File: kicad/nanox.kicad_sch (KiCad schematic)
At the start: 138 parts, among them P1 likely an ESD protection diod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, P2 likely an ESD protection diod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, P3 likely an ESD protection diod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, P4 likely an ESD protection diod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, P5 likely an ESD protection diod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, SW1 push button, left, SW2 push button, right, X1 ?, X10 unknown, marked 1C4F, likely 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, X2 unknown, marked 2GC, X3 unknown, marked 6, X4 ?, X5 ?, X6 ?, X7 ?, X8 ?, X9 unknown, marked P8W 26, Y1 crystal, likely the 32 MHz HSE

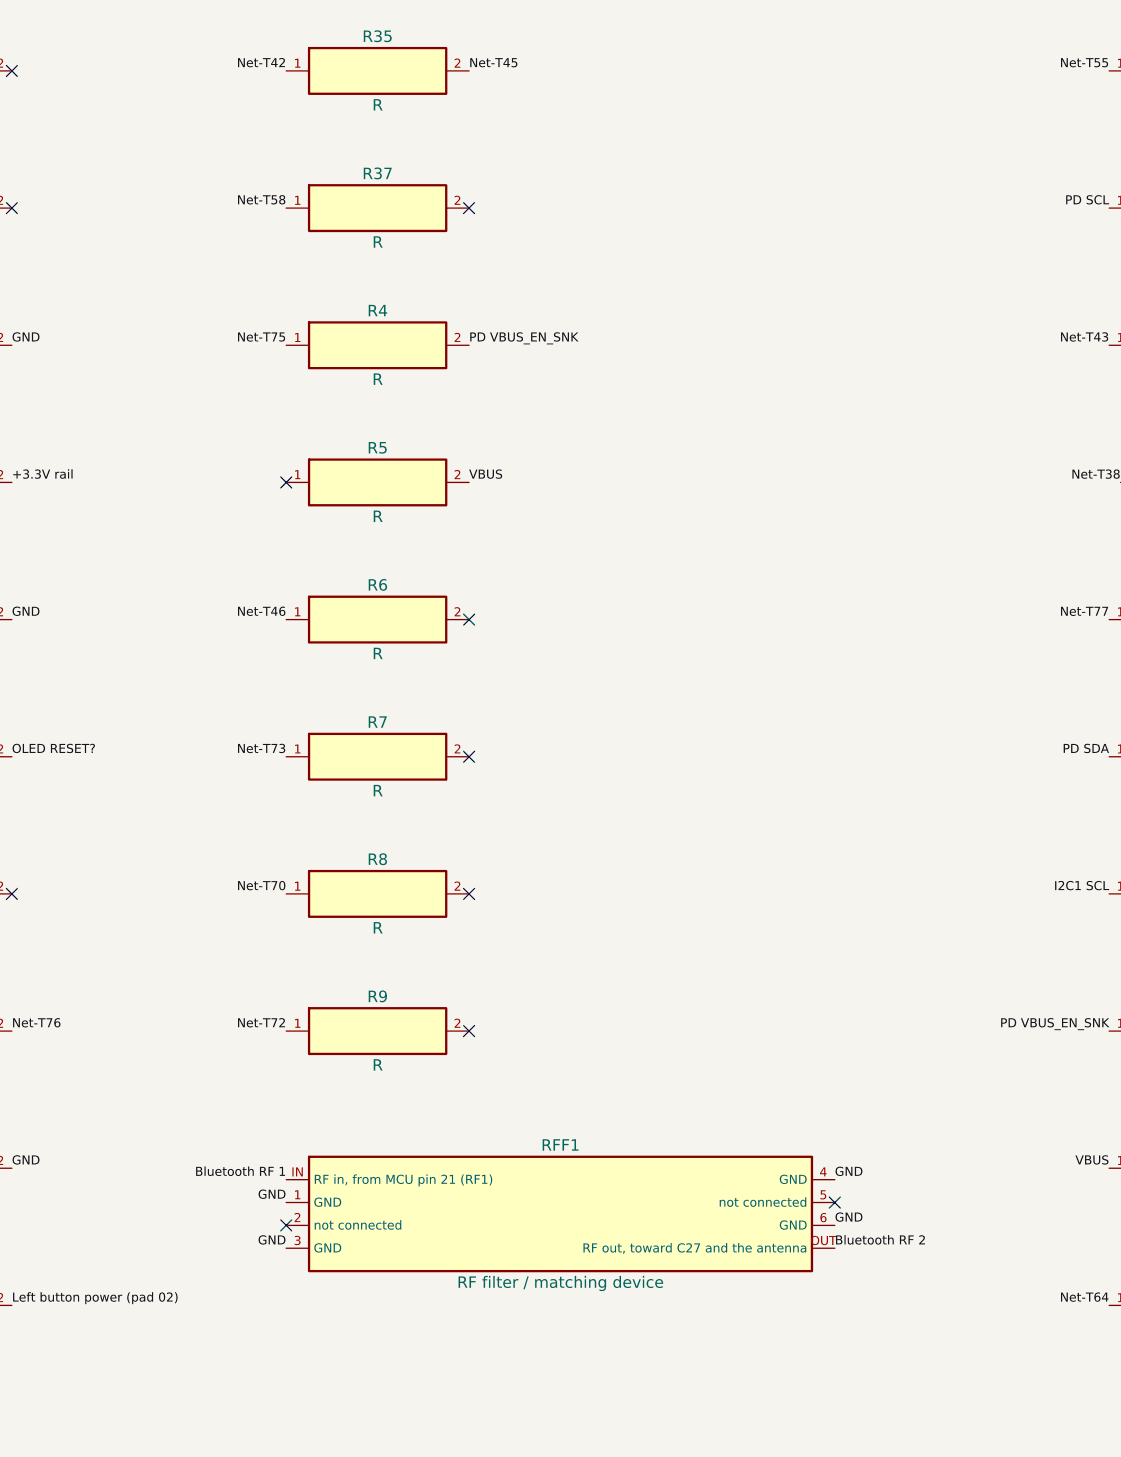
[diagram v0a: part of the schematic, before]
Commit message: Remove R37, a duplicate of R19
R37 was added by hand on the resistor below R18, which the automatic
pass had already found as R19. R19 keeps R37's better-fitting box.

Co-Authored-By: Claude Opus 5.5 <noreply@anthropic.com>
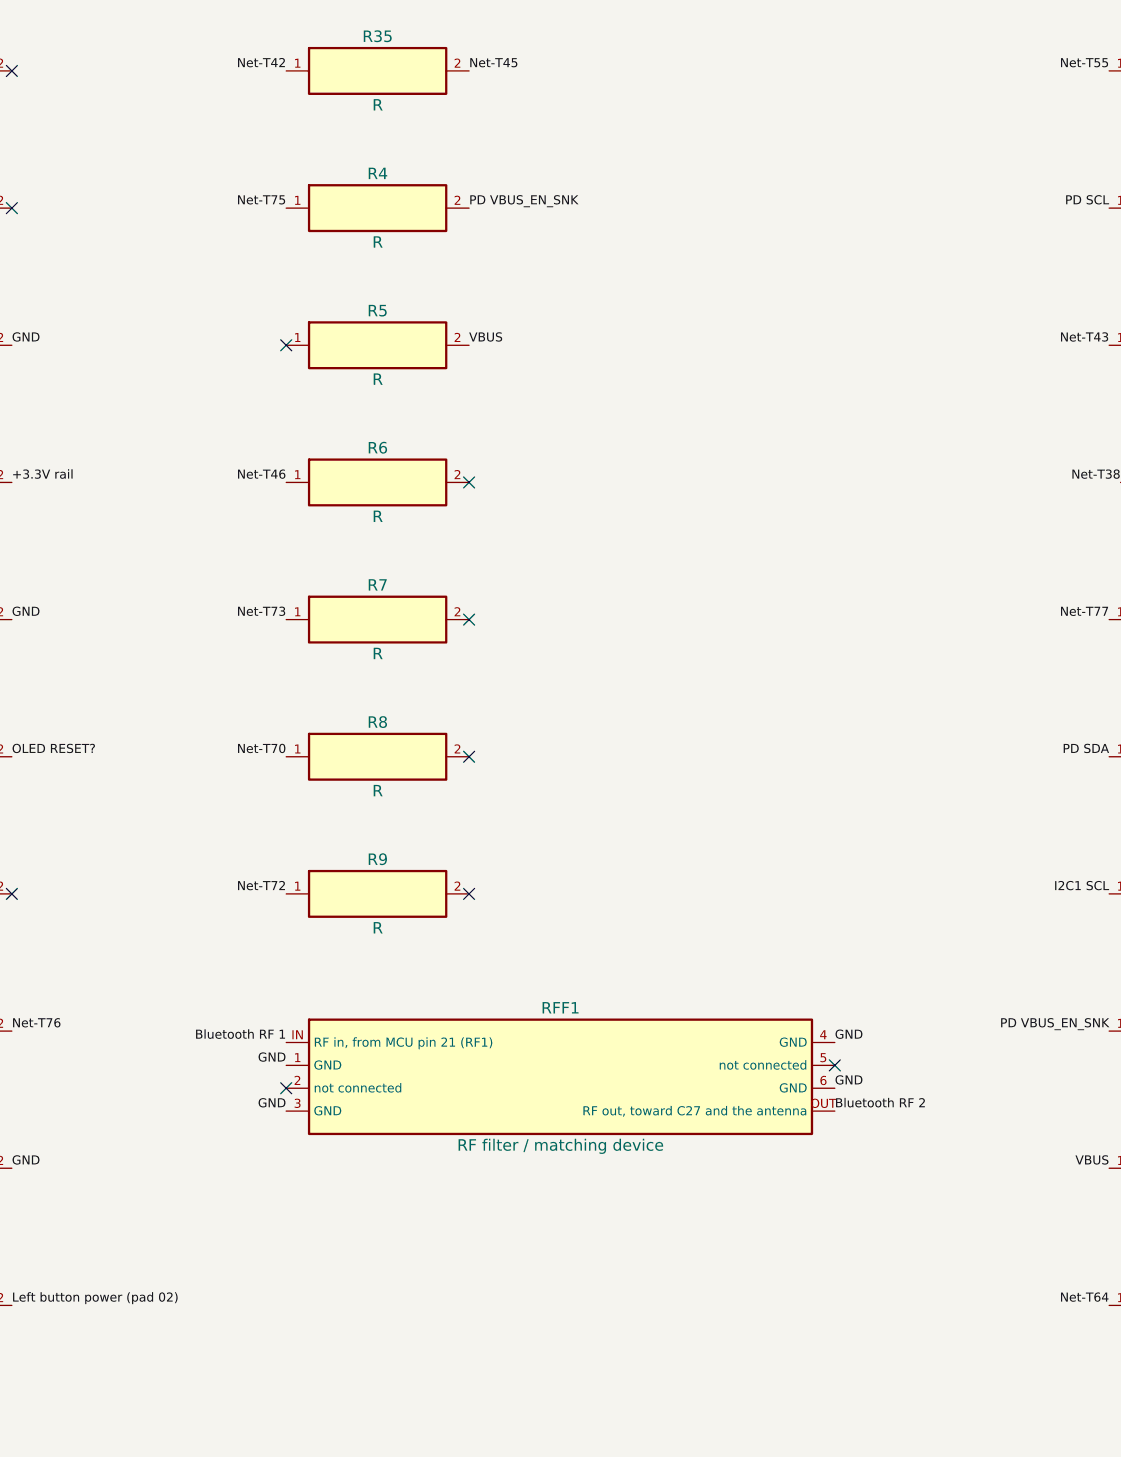
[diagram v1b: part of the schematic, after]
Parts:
- removed R37: R, symbol nanox:R37
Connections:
- no-connect marks 73 -> 72
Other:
- moved on the sheet: R4, R5, R6, R7, R8, R9, RFF1
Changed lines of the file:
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@@
  (label "Net-T42" (at 236.22 149.86 180) (effects (font (size 1.0 1.0)) (justify right bottom)))
  (label "Net-T45" (at 256.54 149.86 0) (effects (font (size 1.0 1.0)) (justify left bottom)))
- (symbol (lib_id "nanox:R37") (at 246.38 165.10 0) (unit 1) (in_bom yes) (on_board yes) (dnp no)
-  (property "Reference" "R37" (at 246.38 161.29 0) (effects (font (size 1.27 1.27))))
+ (symbol (lib_id "nanox:R4") (at 246.38 165.10 0) (unit 1) (in_bom yes) (on_board yes) (dnp no)
+  (property "Reference" "R4" (at 246.38 161.29 0) (effects (font (size 1.27 1.27))))
   (property "Value" "R" (at 246.38 168.91 0) (effects (font (size 1.27 1.27))))
   (property "Footprint" "" (at 246.38 165.10 0) (effects (font (size 1.27 1.27)) hide))
@@
   (pin "1")
   (pin "2")
-  (instances (project "nanox" (path "/9fc871f3-1e36-5a01-9359-e2a20c86f96f" (reference "R37") (unit 1))))
+  (instances (project "nanox" (path "/9fc871f3-1e36-5a01-9359-e2a20c86f96f" (reference "R4") (unit 1))))
  )
- (label "Net-T58" (at 236.22 165.10 180) (effects (font (size 1.0 1.0)) (justify right bottom)))
- (no_connect (at 256.54 165.10))
- (symbol (lib_id "nanox:R4") (at 246.38 180.34 0) (unit 1) (in_bom yes) (on_board yes) (dnp no)
-  (property "Reference" "R4" (at 246.38 176.53 0) (effects (font (size 1.27 1.27))))
+ (label "Net-T75" (at 236.22 165.10 180) (effects (font (size 1.0 1.0)) (justify right bottom)))
+ (label "PD VBUS_EN_SNK" (at 256.54 165.10 0) (effects (font (size 1.0 1.0)) (justify left bottom)))
+ (symbol (lib_id "nanox:R5") (at 246.38 180.34 0) (unit 1) (in_bom yes) (on_board yes) (dnp no)
+  (property "Reference" "R5" (at 246.38 176.53 0) (effects (font (size 1.27 1.27))))
   (property "Value" "R" (at 246.38 184.15 0) (effects (font (size 1.27 1.27))))
   (property "Footprint" "" (at 246.38 180.34 0) (effects (font (size 1.27 1.27)) hide))
@@
   (pin "1")
   (pin "2")
-  (instances (project "nanox" (path "/9fc871f3-1e36-5a01-9359-e2a20c86f96f" (reference "R4") (unit 1))))
+  (instances (project "nanox" (path "/9fc871f3-1e36-5a01-9359-e2a20c86f96f" (reference "R5") (unit 1))))
  )
- (label "Net-T75" (at 236.22 180.34 180) (effects (font (size 1.0 1.0)) (justify right bottom)))
- (label "PD VBUS_EN_SNK" (at 256.54 180.34 0) (effects (font (size 1.0 1.0)) (justify left bottom)))
- (symbol (lib_id "nanox:R5") (at 246.38 195.58 0) (unit 1) (in_bom yes) (on_board yes) (dnp no)
-  (property "Reference" "R5" (at 246.38 191.77 0) (effects (font (size 1.27 1.27))))
+ (no_connect (at 236.22 180.34))
+ (label "VBUS" (at 256.54 180.34 0) (effects (font (size 1.0 1.0)) (justify left bottom)))
+ (symbol (lib_id "nanox:R6") (at 246.38 195.58 0) (unit 1) (in_bom yes) (on_board yes) (dnp no)
+  (property "Reference" "R6" (at 246.38 191.77 0) (effects (font (size 1.27 1.27))))
   (property "Value" "R" (at 246.38 199.39 0) (effects (font (size 1.27 1.27))))
   (property "Footprint" "" (at 246.38 195.58 0) (effects (font (size 1.27 1.27)) hide))
@@
   (pin "1")
   (pin "2")
-  (instances (project "nanox" (path "/9fc871f3-1e36-5a01-9359-e2a20c86f96f" (reference "R5") (unit 1))))
+  (instances (project "nanox" (path "/9fc871f3-1e36-5a01-9359-e2a20c86f96f" (reference "R6") (unit 1))))
  )
- (no_connect (at 236.22 195.58))
- (label "VBUS" (at 256.54 195.58 0) (effects (font (size 1.0 1.0)) (justify left bottom)))
- (symbol (lib_id "nanox:R6") (at 246.38 210.82 0) (unit 1) (in_bom yes) (on_board yes) (dnp no)
-  (property "Reference" "R6" (at 246.38 207.01 0) (effects (font (size 1.27 1.27))))
+ (label "Net-T46" (at 236.22 195.58 180) (effects (font (size 1.0 1.0)) (justify right bottom)))
+ (no_connect (at 256.54 195.58))
+ (symbol (lib_id "nanox:R7") (at 246.38 210.82 0) (unit 1) (in_bom yes) (on_board yes) (dnp no)
+  (property "Reference" "R7" (at 246.38 207.01 0) (effects (font (size 1.27 1.27))))
   (property "Value" "R" (at 246.38 214.63 0) (effects (font (size 1.27 1.27))))
   (property "Footprint" "" (at 246.38 210.82 0) (effects (font (size 1.27 1.27)) hide))
@@
   (pin "1")
   (pin "2")
-  (instances (project "nanox" (path "/9fc871f3-1e36-5a01-9359-e2a20c86f96f" (reference "R6") (unit 1))))
+  (instances (project "nanox" (path "/9fc871f3-1e36-5a01-9359-e2a20c86f96f" (reference "R7") (unit 1))))
  )
- (label "Net-T46" (at 236.22 210.82 180) (effects (font (size 1.0 1.0)) (justify right bottom)))
+ (label "Net-T73" (at 236.22 210.82 180) (effects (font (size 1.0 1.0)) (justify right bottom)))
  (no_connect (at 256.54 210.82))
- (symbol (lib_id "nanox:R7") (at 246.38 226.06 0) (unit 1) (in_bom yes) (on_board yes) (dnp no)
-  (property "Reference" "R7" (at 246.38 222.25 0) (effects (font (size 1.27 1.27))))
+ (symbol (lib_id "nanox:R8") (at 246.38 226.06 0) (unit 1) (in_bom yes) (on_board yes) (dnp no)
+  (property "Reference" "R8" (at 246.38 222.25 0) (effects (font (size 1.27 1.27))))
   (property "Value" "R" (at 246.38 229.87 0) (effects (font (size 1.27 1.27))))
   (property "Footprint" "" (at 246.38 226.06 0) (effects (font (size 1.27 1.27)) hide))
@@
   (pin "1")
   (pin "2")
-  (instances (project "nanox" (path "/9fc871f3-1e36-5a01-9359-e2a20c86f96f" (reference "R7") (unit 1))))
+  (instances (project "nanox" (path "/9fc871f3-1e36-5a01-9359-e2a20c86f96f" (reference "R8") (unit 1))))
  )
- (label "Net-T73" (at 236.22 226.06 180) (effects (font (size 1.0 1.0)) (justify right bottom)))
+ (label "Net-T70" (at 236.22 226.06 180) (effects (font (size 1.0 1.0)) (justify right bottom)))
  (no_connect (at 256.54 226.06))
- (symbol (lib_id "nanox:R8") (at 246.38 241.30 0) (unit 1) (in_bom yes) (on_board yes) (dnp no)
-  (property "Reference" "R8" (at 246.38 237.49 0) (effects (font (size 1.27 1.27))))
+ (symbol (lib_id "nanox:R9") (at 246.38 241.30 0) (unit 1) (in_bom yes) (on_board yes) (dnp no)
+  (property "Reference" "R9" (at 246.38 237.49 0) (effects (font (size 1.27 1.27))))
   (property "Value" "R" (at 246.38 245.11 0) (effects (font (size 1.27 1.27))))
   (property "Footprint" "" (at 246.38 241.30 0) (effects (font (size 1.27 1.27)) hide))
@@
   (pin "1")
   (pin "2")
-  (instances (project "nanox" (path "/9fc871f3-1e36-5a01-9359-e2a20c86f96f" (reference "R8") (unit 1))))
- )
- (label "Net-T70" (at 236.22 241.30 180) (effects (font (size 1.0 1.0)) (justify right bottom)))
- (no_connect (at 256.54 241.30))
- (symbol (lib_id "nanox:R9") (at 246.38 256.54 0) (unit 1) (in_bom yes) (on_board yes) (dnp no)
-  (property "Reference" "R9" (at 246.38 252.73 0) (effects (font (size 1.27 1.27))))
-  (property "Value" "R" (at 246.38 260.35 0) (effects (font (size 1.27 1.27))))
-  (property "Footprint" "" (at 246.38 256.54 0) (effects (font (size 1.27 1.27)) hide))
-  (property "Description" "two-terminal SMD" (at 246.38 256.54 0) (effects (font (size 1.27 1.27)) hide))
-  (pin "1")
-  (pin "2")
   (instances (project "nanox" (path "/9fc871f3-1e36-5a01-9359-e2a20c86f96f" (reference "R9") (unit 1))))
  )
- (label "Net-T72" (at 236.22 256.54 180) (effects (font (size 1.0 1.0)) (justify right bottom)))
- (no_connect (at 256.54 256.54))
- (symbol (lib_id "nanox:RFF1") (at 266.70 276.86 0) (unit 1) (in_bom yes) (on_board yes) (dnp no)
-  (property "Reference" "RFF1" (at 266.70 269.24 0) (effects (font (size 1.27 1.27))))
-  (property "Value" "RF filter / matching device" (at 266.70 284.48 0) (effects (font (size 1.27 1.27))))
-  (property "Footprint" "" (at 266.70 276.86 0) (effects (font (size 1.27 1.27)) hide))
-  (property "Description" "blue ceramic, 8 terminals" (at 266.70 276.86 0) (effects (font (size 1.27 1.27)) hide))
+ (label "Net-T72" (at 236.22 241.30 180) (effects (font (size 1.0 1.0)) (justify right bottom)))
+ (no_connect (at 256.54 241.30))
+ (symbol (lib_id "nanox:RFF1") (at 266.70 261.62 0) (unit 1) (in_bom yes) (on_board yes) (dnp no)
+  (property "Reference" "RFF1" (at 266.70 254.00 0) (effects (font (size 1.27 1.27))))
+  (property "Value" "RF filter / matching device" (at 266.70 269.24 0) (effects (font (size 1.27 1.27))))
+  (property "Footprint" "" (at 266.70 261.62 0) (effects (font (size 1.27 1.27)) hide))
+  (property "Description" "blue ceramic, 8 terminals" (at 266.70 261.62 0) (effects (font (size 1.27 1.27)) hide))
   (pin "IN")
   (pin "1")
@@
   (instances (project "nanox" (path "/9fc871f3-1e36-5a01-9359-e2a20c86f96f" (reference "RFF1") (unit 1))))
  )
- (label "Bluetooth RF 1" (at 236.22 273.05 180) (effects (font (size 1.0 1.0)) (justify right bottom)))
- (label "GND" (at 236.22 275.59 180) (effects (font (size 1.0 1.0)) (justify right bottom)))
- (no_connect (at 236.22 278.13))
- (label "GND" (at 236.22 280.67 180) (effects (font (size 1.0 1.0)) (justify right bottom)))
- (label "GND" (at 297.18 273.05 0) (effects (font (size 1.0 1.0)) (justify left bottom)))
- (no_connect (at 297.18 275.59))
- (label "GND" (at 297.18 278.13 0) (effects (font (size 1.0 1.0)) (justify left bottom)))
- (label "Bluetooth RF 2" (at 297.18 280.67 0) (effects (font (size 1.0 1.0)) (justify left bottom)))
+ (label "Bluetooth RF 1" (at 236.22 257.81 180) (effects (font (size 1.0 1.0)) (justify right bottom)))
+ (label "GND" (at 236.22 260.35 180) (effects (font (size 1.0 1.0)) (justify right bottom)))
+ (no_connect (at 236.22 262.89))
+ (label "GND" (at 236.22 265.43 180) (effects (font (size 1.0 1.0)) (justify right bottom)))
+ (label "GND" (at 297.18 257.81 0) (effects (font (size 1.0 1.0)) (justify left bottom)))
+ (no_connect (at 297.18 260.35))
+ (label "GND" (at 297.18 262.89 0) (effects (font (size 1.0 1.0)) (justify left bottom)))
+ (label "Bluetooth RF 2" (at 297.18 265.43 0) (effects (font (size 1.0 1.0)) (justify left bottom)))
  (symbol (lib_id "nanox:SE1") (at 337.82 40.64 0) (unit 1) (in_bom yes) (on_board yes) (dnp no)
   (property "Reference" "SE1" (at 337.82 24.13 0) (effects (font (size 1.27 1.27))))

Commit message: Connect C14, C7, R9 and R13 to the traces over them
They were flagged as overlaps but the traces really end on them: the
+3.3V rail on C14, trace 38 on C7, and trace 41 on R9 and R13.

Co-Authored-By: Claude Opus 5.5 <noreply@anthropic.com>
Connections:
- net +3.3V rail: now also C14.2
- net Net-T38: now also C7.1
- net Net-T41: now also R13.1, R9.2
- no-connect marks 72 -> 68
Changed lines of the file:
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@@
  )
  (label "GND" (at 25.40 175.26 180) (effects (font (size 1.0 1.0)) (justify right bottom)))
- (no_connect (at 45.72 175.26))
+ (label "+3.3V rail" (at 45.72 175.26 0) (effects (font (size 1.0 1.0)) (justify left bottom)))
  (symbol (lib_id "nanox:C15") (at 35.56 190.50 0) (unit 1) (in_bom yes) (on_board yes) (dnp no)
   (property "Reference" "C15" (at 35.56 186.69 0) (effects (font (size 1.27 1.27))))
@@
   (instances (project "nanox" (path "/9fc871f3-1e36-5a01-9359-e2a20c86f96f" (reference "C7") (unit 1))))
  )
- (no_connect (at 76.20 271.78))
+ (label "Net-T38" (at 76.20 271.78 180) (effects (font (size 1.0 1.0)) (justify right bottom)))
  (label "GND" (at 96.52 271.78 0) (effects (font (size 1.0 1.0)) (justify left bottom)))
  (symbol (lib_id "nanox:C8") (at 86.36 287.02 0) (unit 1) (in_bom yes) (on_board yes) (dnp no)
@@
   (instances (project "nanox" (path "/9fc871f3-1e36-5a01-9359-e2a20c86f96f" (reference "R13") (unit 1))))
  )
- (no_connect (at 185.42 73.66))
+ (label "Net-T41" (at 185.42 73.66 180) (effects (font (size 1.0 1.0)) (justify right bottom)))
  (no_connect (at 205.74 73.66))
  (symbol (lib_id "nanox:R14") (at 195.58 88.90 0) (unit 1) (in_bom yes) (on_board yes) (dnp no)
@@
  )
  (label "Net-T72" (at 236.22 241.30 180) (effects (font (size 1.0 1.0)) (justify right bottom)))
- (no_connect (at 256.54 241.30))
+ (label "Net-T41" (at 256.54 241.30 0) (effects (font (size 1.0 1.0)) (justify left bottom)))
  (symbol (lib_id "nanox:RFF1") (at 266.70 261.62 0) (unit 1) (in_bom yes) (on_board yes) (dnp no)
   (property "Reference" "RFF1" (at 266.70 254.00 0) (effects (font (size 1.27 1.27))))

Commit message: Connect trace 65 to R13
Trace 65 ran through R13's free end without a point on it; it does
connect there, so the run gets a point on the pad.

Co-Authored-By: Claude Opus 5.5 <noreply@anthropic.com>
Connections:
- net Net-T65: now also R13.2
- no-connect marks 68 -> 67
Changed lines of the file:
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@@
  )
  (label "Net-T41" (at 185.42 73.66 180) (effects (font (size 1.0 1.0)) (justify right bottom)))
- (no_connect (at 205.74 73.66))
+ (label "Net-T65" (at 205.74 73.66 0) (effects (font (size 1.0 1.0)) (justify left bottom)))
  (symbol (lib_id "nanox:R14") (at 195.58 88.90 0) (unit 1) (in_bom yes) (on_board yes) (dnp no)
   (property "Reference" "R14" (at 195.58 85.09 0) (effects (font (size 1.27 1.27))))

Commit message: Fix R14's position and connect R19 to the +3.3V rail
The previous commit put R14's box 1000 px too low by a typo, leaving it
unconnected; it now sits on its real pads, joining trace 37 and GND.
R19's right end gets a stub from the +3.3V rail, whose bend sat
exactly on the pad's edge.

Co-Authored-By: Claude Opus 5.5 <noreply@anthropic.com>
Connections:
- net +3.3V rail: now also R19.2
- net GND: now also R14.2
- net Net-T37: now also R14.1
- no-connect marks 67 -> 64
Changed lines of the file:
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@@
   (instances (project "nanox" (path "/9fc871f3-1e36-5a01-9359-e2a20c86f96f" (reference "R14") (unit 1))))
  )
- (no_connect (at 185.42 88.90))
- (no_connect (at 205.74 88.90))
+ (label "Net-T37" (at 185.42 88.90 180) (effects (font (size 1.0 1.0)) (justify right bottom)))
+ (label "GND" (at 205.74 88.90 0) (effects (font (size 1.0 1.0)) (justify left bottom)))
  (symbol (lib_id "nanox:R15") (at 195.58 104.14 0) (unit 1) (in_bom yes) (on_board yes) (dnp no)
   (property "Reference" "R15" (at 195.58 100.33 0) (effects (font (size 1.27 1.27))))
@@
  )
  (label "Net-T58" (at 185.42 165.10 180) (effects (font (size 1.0 1.0)) (justify right bottom)))
- (no_connect (at 205.74 165.10))
+ (label "+3.3V rail" (at 205.74 165.10 0) (effects (font (size 1.0 1.0)) (justify left bottom)))
  (symbol (lib_id "nanox:R20") (at 195.58 180.34 0) (unit 1) (in_bom yes) (on_board yes) (dnp no)
   (property "Reference" "R20" (at 195.58 176.53 0) (effects (font (size 1.27 1.27))))
